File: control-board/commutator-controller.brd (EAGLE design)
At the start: 43 x 63 mm, 40 parts, among them U1 IS31FL3193, U2 LTC4425EMSE#PBF, U3 TEENSY_LC, U4 PTN04050C, U5 TMC2130

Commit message: Nearly complete control board
- Silkscreen still needs work: button labels, device label, etc
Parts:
- removed 1.2M, 1.5M: (no value), jonnew:0603
- removed IREF_AIN: (no value), jonnew:TESTPOINT_2MM
- removed J2: (no value), jonnew:1X04
- removed R17: 10k, jonnew:0402
- removed S4: (no value), jonnew:TOUCH-2X2CM
- removed TP1: RESET, jonnew:TESTPOINT_1MM
- added GND1, GND2: (no value), jonnew:B2,54
- added J1: (no value), jonnew:JP4_SMD
- added R11: 500, jonnew:0603
- added R12, R13: 4.7k, jonnew:0603
- +3.3V, +5V, +5V1, GND: device jonnew:TESTPOINT_2MM -> jonnew:B2,54
- C10: value 22uF -> 1F; device jonnew:1206 -> jonnew:1210-POL
- C2: value 10nF -> 22uF; device jonnew:0402 -> jonnew:1206
- C3: value 1uF/50V -> 22uF; device jonnew:0603 -> jonnew:1206
- C5: value 1F -> 100 uF; device jonnew:1210-POL -> jonnew:153CLV-0807
- C6: value 2.2uF -> 100uF; device jonnew:0805 -> jonnew:153CLV-0807
- C7: value 100uF -> 2.2uF; device jonnew:153CLV-0807 -> jonnew:0805
- C8: value 100 uF -> 10nF; device jonnew:153CLV-0807 -> jonnew:0402
- C9: value 22uF -> 1uF; device jonnew:1206 -> jonnew:0603
- R1: device jonnew:0402 -> jonnew:0603
- R10, R9: value 4.7k -> 10k; device jonnew:0402 -> jonnew:0603
- R2: value 10k -> 1.5M
- R3: value 10k -> 1.33k
- R4: value 0 -> 1.2M
- R5: value DNP -> 0
- R6: value 10k -> DNP
- R7: value 1.33k -> 10k
- R8: value 500 -> 10k
- S1, S2: device jonnew:EVQP7 -> jonnew:TOUCH-2X2CM
- S3: device jonnew:TOUCH-2X2CM -> jonnew:EVQP7
- U1: value IS31FL3193 -> PTN04050C; device jonnew:PWSON-N10-3X3 -> jonnew:PDSS-B4-MODULE
- U3: value TEENSY_LC -> IS31FL3193; device jonnew:TEENSY_LC_SMD -> jonnew:PWSON-N10-3X3
- U4: value PTN04050C -> TMC2130; device jonnew:PDSS-B4-MODULE -> jonnew:SILENT-STEPPER-STICK-SMD
- U5: value TMC2130 -> TEENSY_LC; device jonnew:SILENT-STEPPER-STICK-SMD -> jonnew:TEENSY_LC_SMD
- moved +3.3V 183.5 mm to (5.00, 81.2)
- moved GND 176.3 mm to (8.30, 89.2)
- moved C9 165.9 mm to (35.4, 90.2), turned to 270 degrees
- moved R7 161.7 mm to (33.9, 57.6), turned to 90 degrees
- moved C8 157.4 mm to (33.6, 90.6), turned to 270 degrees
- moved C1 147.6 mm to (21.5, 86.3), flipped to the top, turned to 180 degrees
- moved +5V 146.2 mm to (33.8, 42.1)
- moved +5V1 140.1 mm to (40.5, 59.9)
- moved C10 140.0 mm to (30.0, 56.5), turned to 90 degrees
- moved C7 123.9 mm to (38.4, 56.0), turned to 90 degrees
- moved U4 105.4 mm to (14.8, 14.1), turned to 90 degrees
- moved U5 92.9 mm to (43.0, 73.0)
- moved R8 66.7 mm to (34.8, 85.9), turned to 0 degrees
- moved S2 58.7 mm to (11.0, 71.4), flipped to the bottom, turned to 0 degrees
- moved U3 49.6 mm to (29.7, 88.8), turned to 270 degrees
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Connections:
- removed net IREF: IREF_AIN.1
- removed net N$23: S2.1, S2.4, TP1.1
- new net CFG-3/!TMC_CS: U4.12, U5.15
- new net DIR: U4.16, U5.14
- new net STEP: U4.15, U5.16
- new net TMC_EN: U4.9, U5.17
- net !IS31_SHDN: now also R8.1, U3.1, U5.2; no longer R17.1, U1.1
- net !PFO: now also R7.1, U5.23; no longer R6.1, U3.2
- net +3V3: now also +3.3V.TP, R1.2, R12.1, R13.1, R7.2, U4.2, U5.3.3, U5.3V3; no longer +3.3V.1, R6.2, U3.3.3, U3.3V3
- net +5V0: now also +5V.TP, C2.1, C5.+, R5.2, U1.2; no longer +5V.1, C8.+, C9.1, R10.1, R4.2, R9.1, U4.2
- net CCW: now also S2.PAD, U5.4; no longer S4.PAD, U3.1
- net CFG-0/MISO: now also U4.13, U5.12; no longer U3.12
- net CFG-1/MOSI: now also U4.10, U5.11; no longer U3.11
- net CFG-2/SCLK: now also U4.11, U5.13; no longer U3.13
- net CHRG_CURR: now also R11.2, U5.21; no longer R8.2
- net CW: now also S1.PAD, U5.0; no longer S3.PAD, U3.0
- net GND: now also C10.-, C6.-, C7.2, C8.2, GND.TP, GND1.TP, GND2.TP, R10.1, R11.1, R6.1, R8.2, R9.1, S3.2, S3.3, U1.1, U3.6, U3.7, U3.PAD, U4.7, U5.GND, U5.GND1, U5.GND2; no longer C10.2, C6.2, C7.-, C8.-, GND.1, R17.2, R2.1, R5.1, R7.1, R8.1, S1.3, S2.2, S2.3, U1.6, U1.7, U1.PAD, U3.GND, U3.GND1, U3.GND2, U5.1, U5.7
- net MOT_POW_EN: now also R10.2, U5.22; no longer R3.2, U3.3
- net N$1: now also R4.1; no longer 1.2M.1
- net N$10: now also U3.4; no longer U1.4
- net N$14: now also C10.+; no longer C5.+
- net N$2: now also R2.1, R4.2; no longer 1.2M.2, 1.5M.1
- net N$3: now also U3.3; no longer U1.3
- net N$4: now also R5.1, R6.2; no longer R4.1, R5.2
- net N$45: now also U3.5; no longer U1.5
- net N$5: now also J1.1, U4.3; no longer J2.1, U5.3
- net N$6: now also J1.2, U4.4; no longer J2.2, U5.4
- net N$7: now also J1.3, U4.5; no longer J2.3, U5.5
- net N$8: now also J1.4, U4.6; no longer J2.4, U5.6
- net N$9: now also R3.2, U1.3; no longer R7.2, U4.3
- net PROGRAM: now also S3.1, S3.4, U5.PROGRAM; no longer S1.1, S1.4, U3.PROGRAM
- net SCL: now also R13.2, U3.8, U5.19; no longer R10.2, U1.8, U3.19
- net SDA: now also R12.2, U3.9, U5.18; no longer R9.2, U1.9, U3.18
- net VCC: now also +5V1.TP, C7.1, C8.1, C9.1, R2.2, U3.2, U5.VIN; no longer +5V1.1, 1.5M.2, C2.1, C3.1, C6.1, R1.2, U1.2, U3.VIN, U5.2
- net VMID_SEL: now also R9.2, U5.20; no longer R2.2, U3.4
- net VMOT: now also C3.1, C6.+, U1.4, U4.8; no longer C10.1, C7.+, U4.4, U5.8
- net V_BM: now also U3.10, U5.3; no longer U1.10
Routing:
- net PROGRAM: track 0.00 -> 107.8 mm
- net +3V3: track 0.00 -> 97.0 mm
- net CFG-1/MOSI: track 0.00 -> 67.3 mm
- net VCC: track 11.7 -> 72.3 mm
- net CFG-0/MISO: track 0.00 -> 59.0 mm
- net DIR: track 0.00 -> 47.2 mm, vias 0 -> 2
- net TMC_EN: track 0.00 -> 46.4 mm
- net CFG-2/SCLK: track 0.00 -> 43.5 mm
- net STEP: track 0.00 -> 43.0 mm, vias 0 -> 2
- net CFG-3/!TMC_CS: track 0.00 -> 42.5 mm, vias 0 -> 2
- net VMOT: track 0.00 -> 40.9 mm
- net GND: track 5.74 -> 35.7 mm, vias 23 -> 112
- net SCL: track 2.68 -> 31.7 mm
- net VMID_SEL: track 0.00 -> 28.6 mm, vias 0 -> 2
- net CHRG_CURR: track 0.00 -> 27.4 mm, vias 0 -> 2
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- added copper zone on layer 1, net +5V0
- added copper zone on layer 2, net GND
- added copper zone on layer 1, net VCC
- removed copper zone on layer 2, net +5V0
- removed copper zone on layer 15, net GND
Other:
- board size 43 x 63 mm -> 43 x 95 mm
- board text added: "Commutator Control Board CERN OHL v1.2 Jon Newman MIT 2019"
- board text removed: "Twister 3 Control Board CERN OHL v1.2 Jon Newman MIT 2018"

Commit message: Completed control board
- Pending review from jvoigts
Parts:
- C10, C4: value 1F -> 3F
- C5: value 100 uF -> 100uF
- S1, S2: device jonnew:TOUCH-2X2CM -> jonnew:TOUCH-1MM
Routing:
- added copper zone on layer 16, net CCW
- added copper zone on layer 16, net CW
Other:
- board text added: "Commutator Control Board CERN OHL v1.2 Jon Newman Jakob Voigts MIT 2019"
- board text added: "Commutator v1.0 OHL v1.2"
- board text added: "HV0820-2R7305-R"
- board text added: "VIN"
- board text removed: "+3.3V"
- board text removed: "+5V"
- board text removed: "Commutator Control Board CERN OHL v1.2 Jon Newman MIT 2019"
- board text removed: "IREF_AIN"

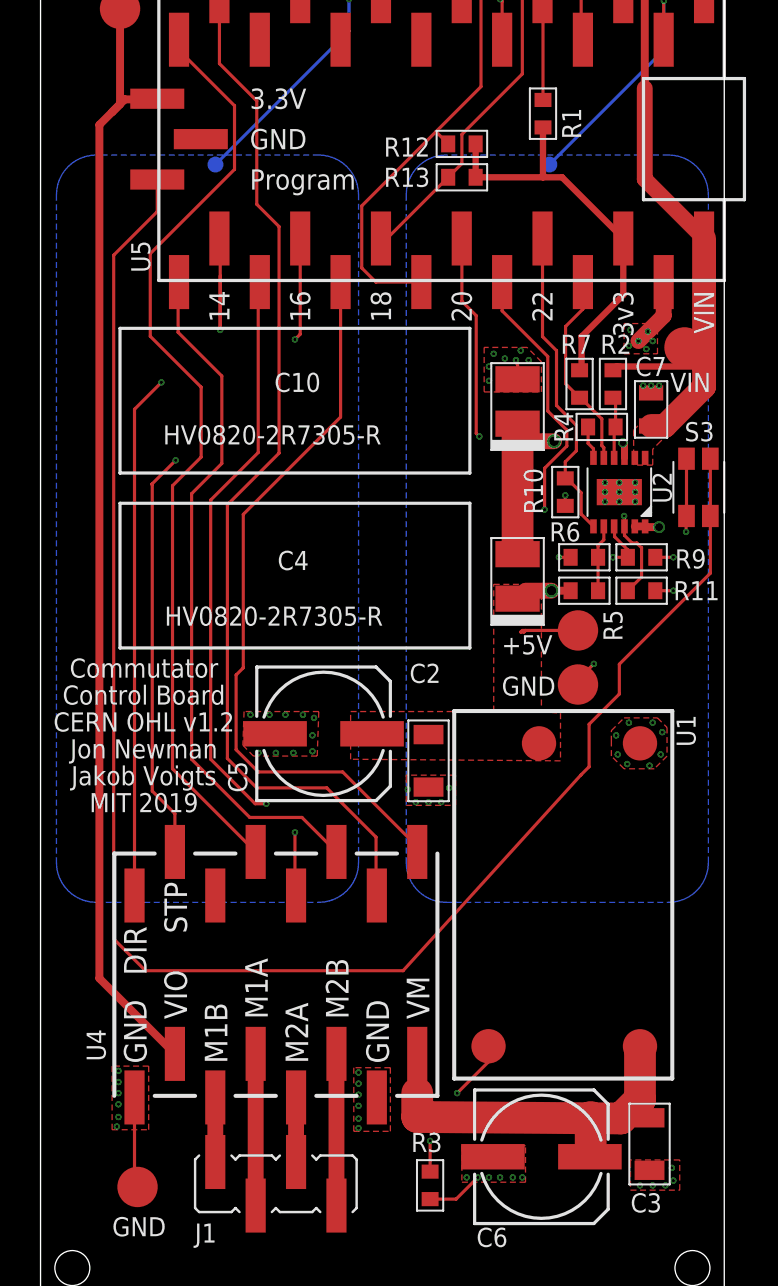
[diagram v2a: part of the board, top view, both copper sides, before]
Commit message: Small updates to control-board after review
- Made sense of rotation direction icons less ambiguous and swapped
positions
- Moved push button back a bit
- Remove copper layer between LED and top side of board
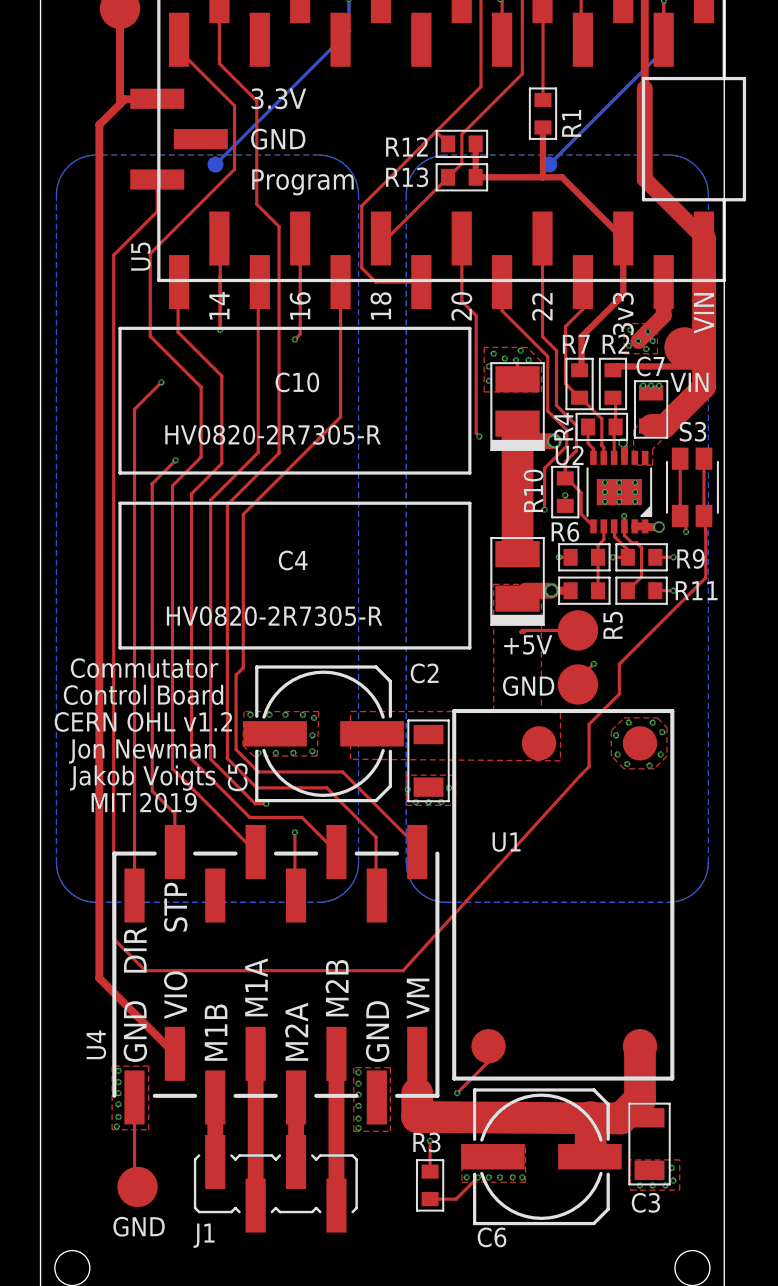
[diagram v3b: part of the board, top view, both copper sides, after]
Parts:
- moved S3 0.40 mm to (41.0, 51.1)
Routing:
- net +3V3: track 97.0 -> 96.3 mm
- added copper zone on layer 2, net N$11
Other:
- board text removed: "- Board to panel stack height: 12 mm. - Teensy goes on bottom with top of teensy facing up (when board is flipped) - Silent stepper stick goes on bottom with top of module facing down (whe board flipped)"

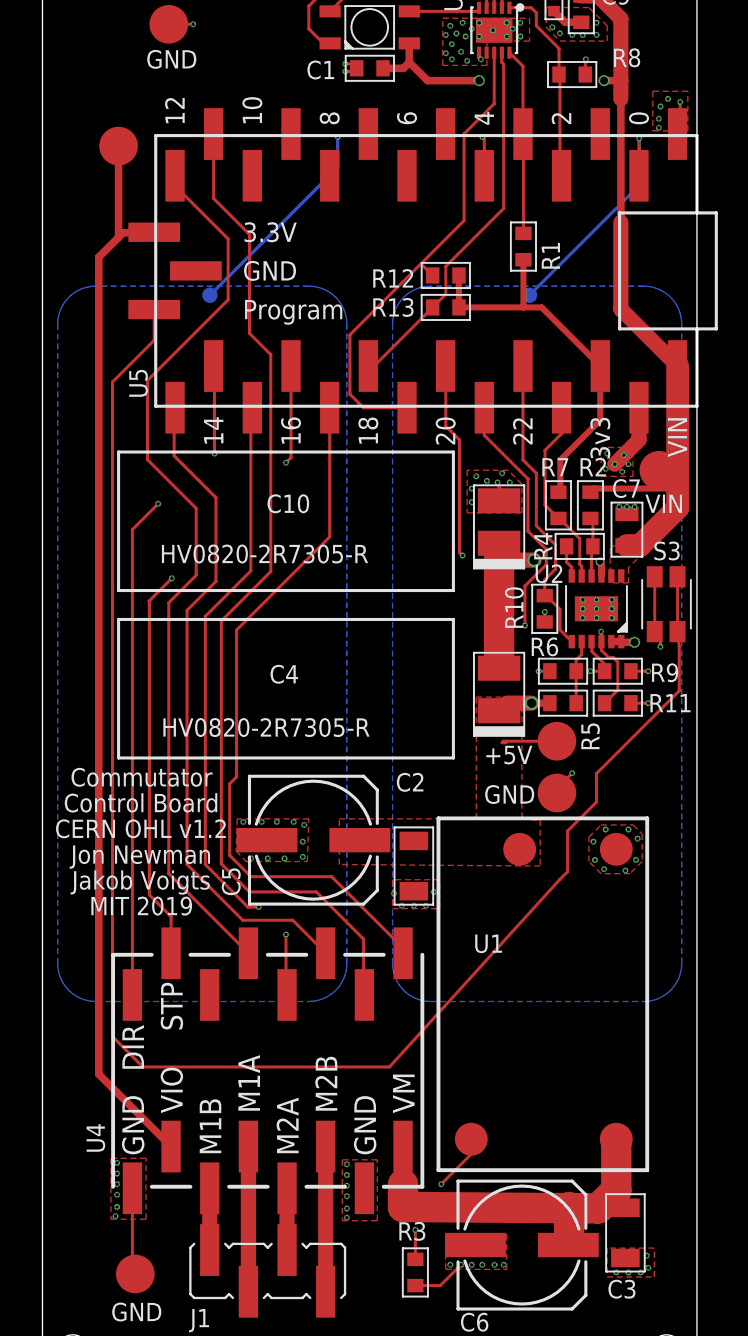
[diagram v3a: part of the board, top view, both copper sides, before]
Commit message: Added stop/go button to control board
- Added README
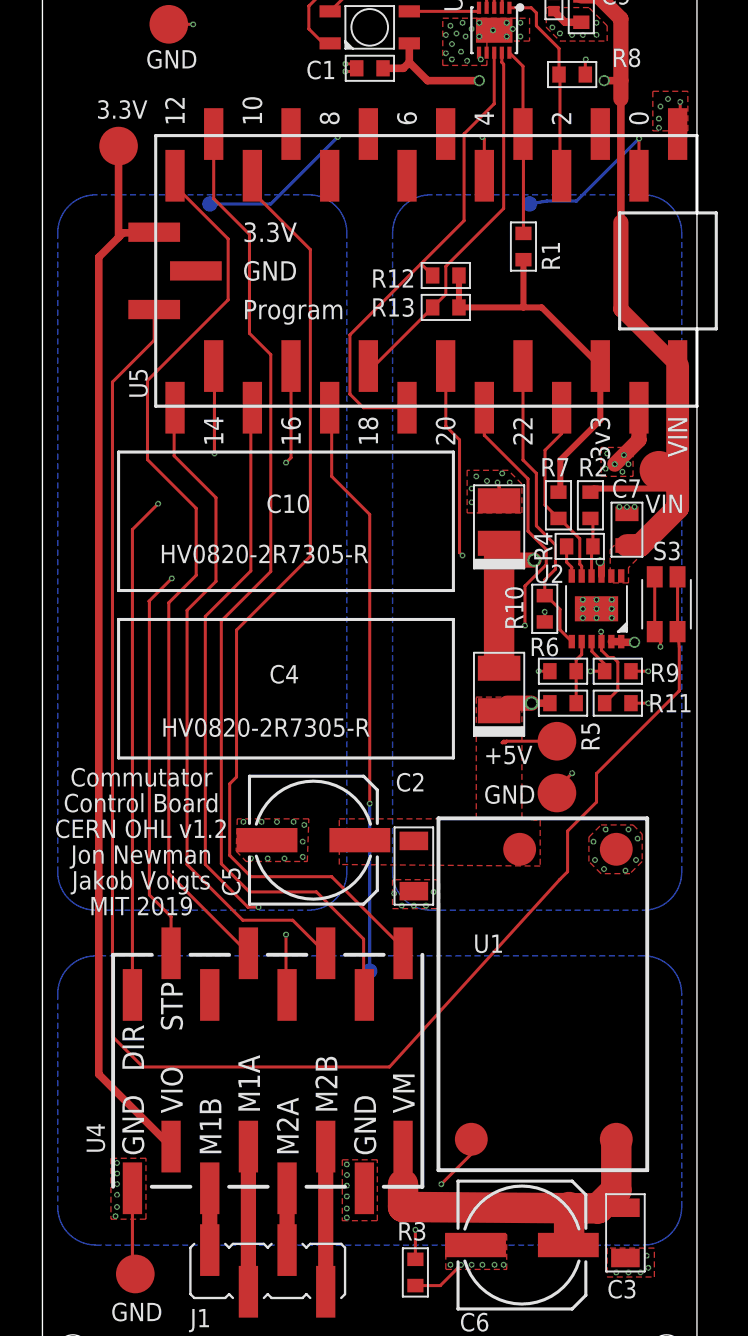
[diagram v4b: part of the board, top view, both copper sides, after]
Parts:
- added S4: (no value), jonnew:TOUCH-1MM
- moved S1 6.00 mm to (32.0, 77.4)
- moved S2 6.00 mm to (11.0, 77.4)
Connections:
- new net STOP: S4.PAD, U5.17
- net TMC_EN: now also U5.10; no longer U5.17
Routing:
- net STOP: track 0.00 -> 38.1 mm, vias 0 -> 1
- net TMC_EN: track 46.4 -> 62.7 mm
- net CW: track 15.7 -> 11.4 mm
- net CCW: track 26.0 -> 22.3 mm
- added copper zone on layer 16, net STOP
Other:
- board text added: "3.3V"

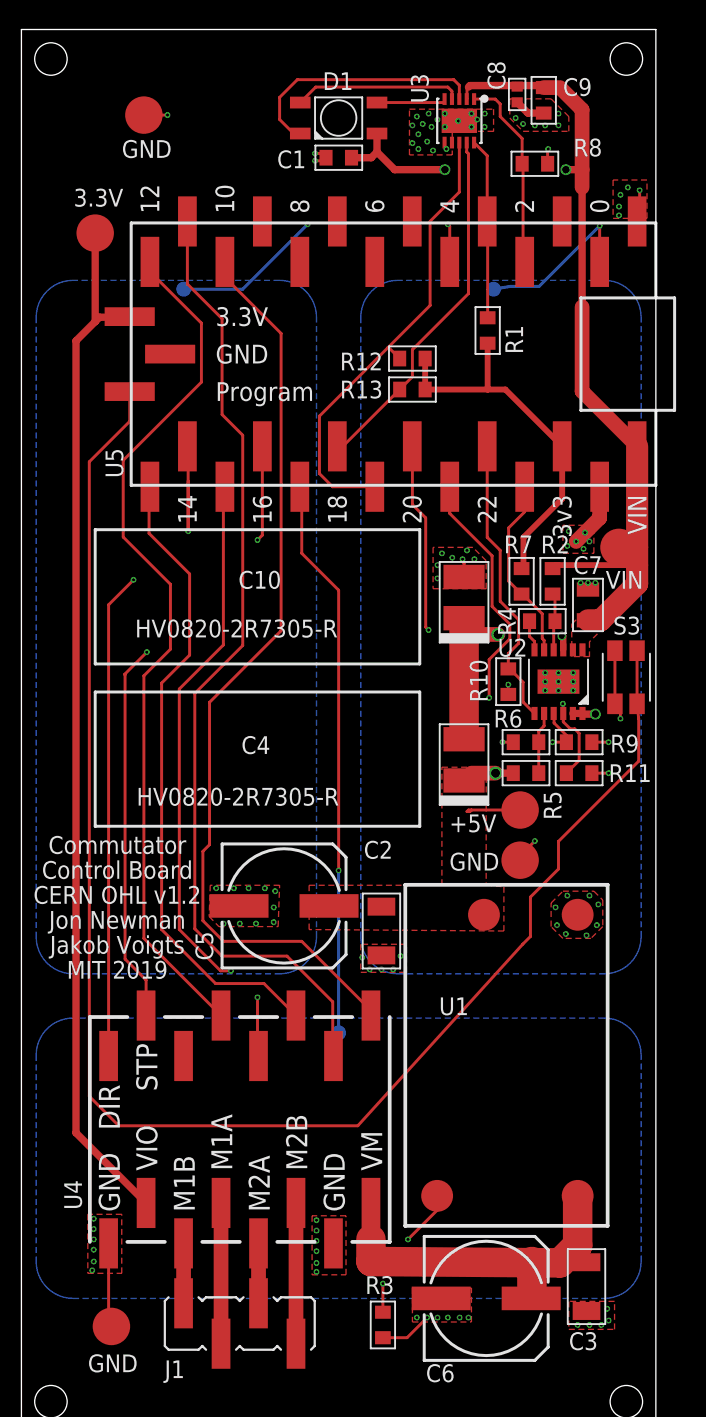
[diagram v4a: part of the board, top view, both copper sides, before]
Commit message: Added fourth mode button on control board
- Sits around RGB LED window
- Also, increased min via drill size to 0.3mm which greatly decreases
board cost
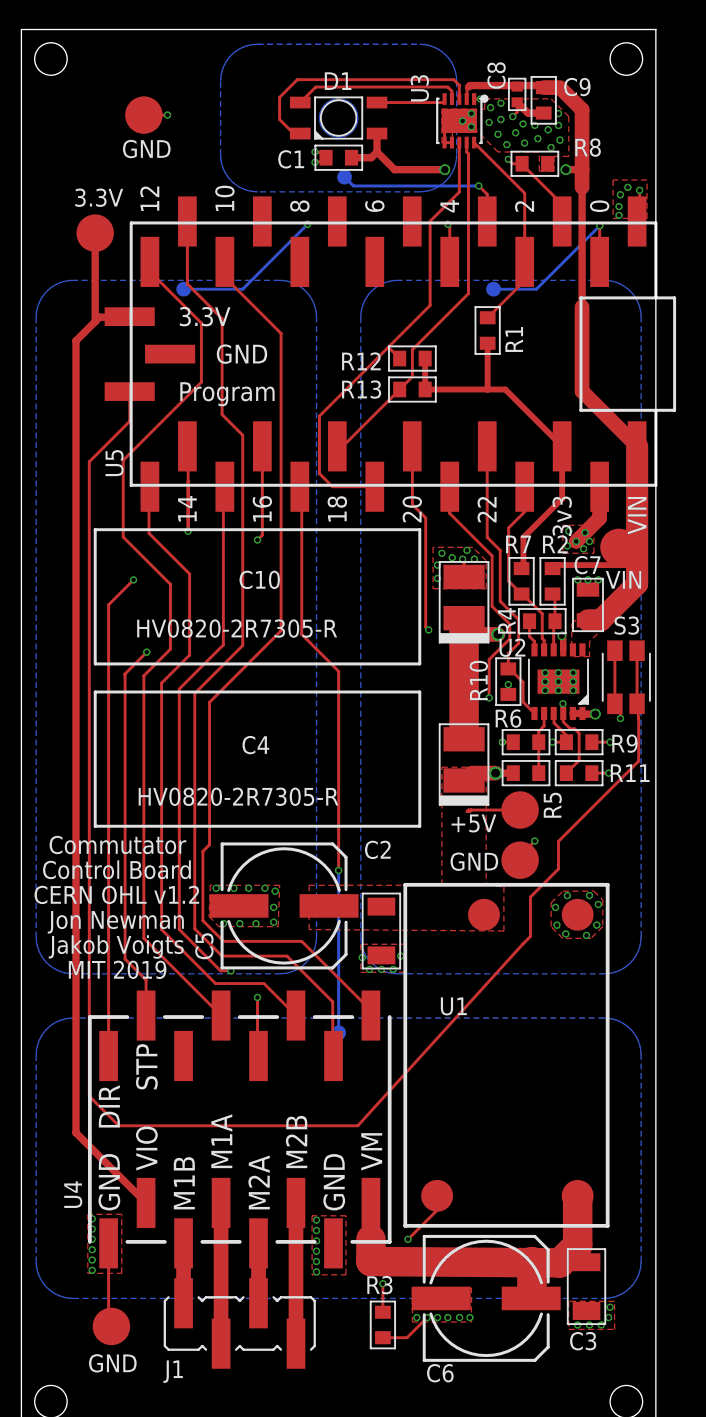
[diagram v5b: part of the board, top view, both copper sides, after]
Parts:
- added S5: (no value), jonnew:TOUCH-1MM
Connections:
- new net MODE: S5.PAD, U5.3
- net !IS31_SHDN: now also U5.1; no longer U5.2
- net V_BM: now also U5.2; no longer U5.3
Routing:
- net MODE: track 0.00 -> 12.0 mm, vias 0 -> 1
- net GND: track 36.0 -> 38.6 mm, vias 112 -> 105
- net V_BM: track 12.3 -> 14.3 mm
- net !IS31_SHDN: track 13.3 -> 11.5 mm, vias 0 -> 2
- added copper zone on layer 16, net MODE
- added copper zone on layer 16, net N$13
